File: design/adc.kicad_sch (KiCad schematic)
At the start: 27 parts, among them J6 JUMPER_DFS/GAIN, U11 TLV431ACDBZR, U12 AD9214

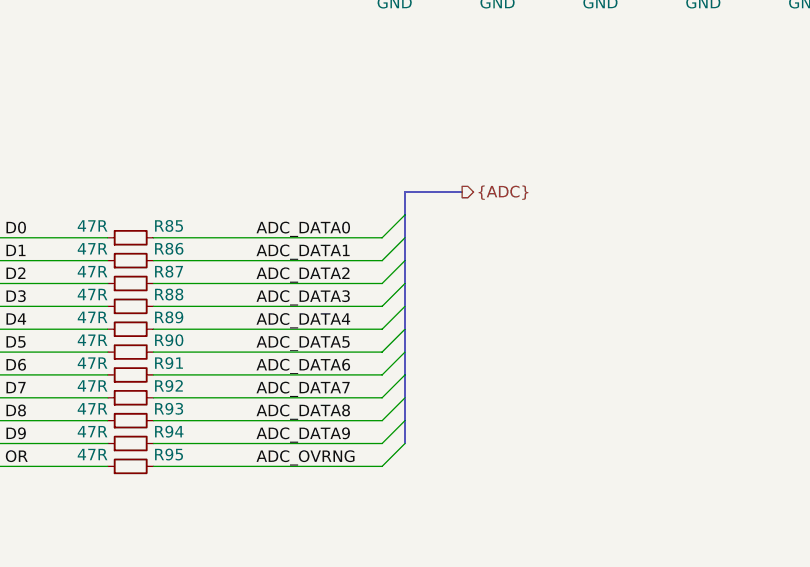
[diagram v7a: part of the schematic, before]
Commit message: Added part SRAM layout
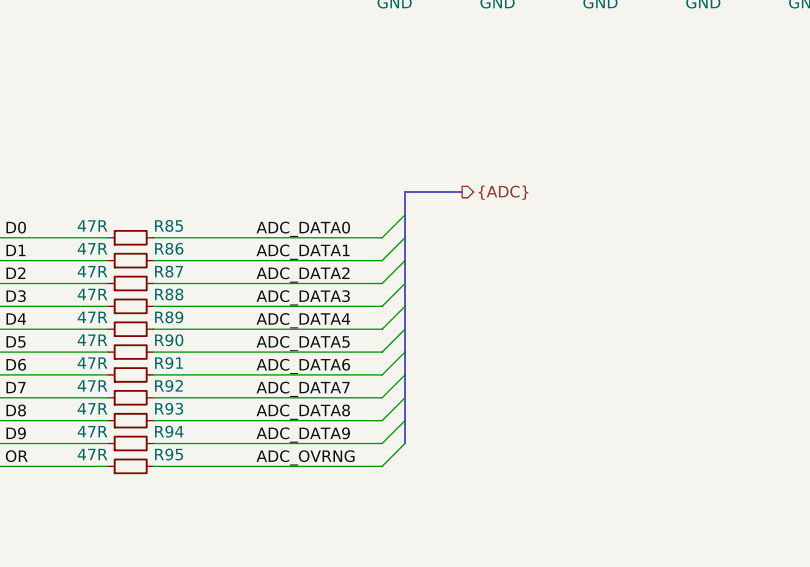
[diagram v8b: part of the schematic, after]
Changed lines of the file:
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@@
-(kicad_sch (version 20200506) (host eeschema "5.99.0-unknown-302646c~101~ubuntu18.04.1")
+(kicad_sch (version 20200506) (host eeschema "5.99.0-unknown-acdfeee~101~ubuntu18.04.1")
   (page "A4")
   (title_block
@@
   )
   (bus_alias "ADC" (members "ADC_DATA[9..0]" "ADC_OVRNG"))
-  (junction (at 248.92 25.4))
+  (junction (at 27.94 36.83))
+  (junction (at 48.26 36.83))
   (junction (at 110.49 130.81))
-  (junction (at 27.94 36.83))
   (junction (at 110.49 133.35))
+  (junction (at 110.49 135.89))
   (junction (at 135.89 138.43))
+  (junction (at 140.97 82.55))
   (junction (at 143.51 82.55))
+  (junction (at 146.05 82.55))
+  (junction (at 146.05 130.81))
   (junction (at 148.59 130.81))
-  (junction (at 259.08 53.34))
-  (junction (at 236.22 53.34))
-  (junction (at 146.05 82.55))
-  (junction (at 270.51 53.34))
-  (junction (at 259.08 25.4))
-  (junction (at 110.49 135.89))
   (junction (at 153.67 82.55))
-  (junction (at 270.51 25.4))
-  (junction (at 140.97 82.55))
-  (junction (at 48.26 36.83))
-  (junction (at 146.05 130.81))
-  (junction (at 247.65 53.34))
   (junction (at 156.21 130.81))
   (junction (at 224.79 53.34))
+  (junction (at 236.22 53.34))
+  (junction (at 247.65 53.34))
+  (junction (at 248.92 25.4))
+  (junction (at 259.08 25.4))
+  (junction (at 259.08 53.34))
+  (junction (at 270.51 25.4))
+  (junction (at 270.51 53.34))
   (no_connect (at 96.52 138.43))
   (bus_entry (at 212.09 93.98) (size 2.54 -2.54))
@@
   (wire (pts (xy 270.51 53.34) (xy 270.51 54.61)))
   (wire (pts (xy 270.51 62.23) (xy 270.51 63.5)))
-  (bus (pts (xy 214.63 88.9) (xy 214.63 91.44)))
-  (bus (pts (xy 214.63 91.44) (xy 214.63 96.52)))
-  (bus (pts (xy 214.63 96.52) (xy 214.63 99.06)))
-  (bus (pts (xy 214.63 99.06) (xy 214.63 104.14)))
-  (bus (pts (xy 214.63 104.14) (xy 214.63 109.22)))
+  (bus (pts (xy 214.63 88.9) (xy 214.63 93.98)))
+  (bus (pts (xy 214.63 93.98) (xy 214.63 96.52)))
+  (bus (pts (xy 214.63 96.52) (xy 214.63 101.6)))
+  (bus (pts (xy 214.63 101.6) (xy 214.63 106.68)))
+  (bus (pts (xy 214.63 106.68) (xy 214.63 109.22)))
   (bus (pts (xy 214.63 109.22) (xy 214.63 114.3)))
   (bus (pts (xy 214.63 114.3) (xy 214.63 116.84)))
